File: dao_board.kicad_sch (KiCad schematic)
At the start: 37 parts, among them J1 KEY1, J10 DISH_SENSOR, J11 5V_BOOST, J12 BATTERY, J13 DISH_LED, J2 KEY2, J3 KEY3, J4 KEY4, J5 KEY5, J6 KEY6, J7 KEY7, J8 START, J9 SELECT, SW1 SW_SPDT, SW2 HX 3x4x2-2P-1.6N, U1 XIAO-nRF52840-Plus-SMD

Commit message: ネット名ミスってて直すなど
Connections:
- net KEY_LED_JV is gone; now on net KEY_LED_5V: D3.1 (K), D4.1 (K)
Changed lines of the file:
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@@
 	(wire
 		(pts
+			(xy 81.28 148.59) (xy 86.36 148.59)
+		)
+		(stroke
+			(width 0)
+			(type default)
+		)
+	)
+	(wire
+		(pts
 			(xy 204.47 31.75) (xy 204.47 40.64)
 		)
@@
 	(wire
 		(pts
-			(xy 86.36 148.59) (xy 59.69 148.59)
+			(xy 81.28 149.86) (xy 59.69 149.86)
 		)
 		(stroke
@@
 	(wire
 		(pts
+			(xy 81.28 149.86) (xy 81.28 148.59)
+		)
+		(stroke
+			(width 0)
+			(type default)
+		)
+	)
+	(wire
+		(pts
 			(xy 167.64 44.45) (xy 181.61 44.45)
 		)
@@
 	(wire
 		(pts
-			(xy 59.69 148.59) (xy 59.69 143.51)
+			(xy 59.69 149.86) (xy 59.69 143.51)
 		)
 		(stroke
@@
 		)
 	)
-	(label "KEY_LED_JV"
+	(label "KEY_LED_5V"
 		(at 107.95 148.59 180)
 		(effects
@@
 		)
 		(instances
-			(project "iidxcontroller_board"
+			(project "dao_board"
 				(path "/88e2b3bc-f15b-46e0-bc23-bfcd5e24d1de"
 					(reference "#PWR019")
@@
 		)
 		(instances
-			(project "iidxcontroller_board"
+			(project "dao_board"
 				(path "/88e2b3bc-f15b-46e0-bc23-bfcd5e24d1de"
 					(reference "J8")
@@
 		)
 		(instances
-			(project "iidxcontroller_board"
+			(project "dao_board"
 				(path "/88e2b3bc-f15b-46e0-bc23-bfcd5e24d1de"
 					(reference "C2")
@@
 		)
 		(instances
-			(project "iidxcontroller_board"
+			(project "dao_board"
 				(path "/88e2b3bc-f15b-46e0-bc23-bfcd5e24d1de"
 					(reference "D3")
@@
 		)
 		(instances
-			(project "iidxcontroller_board"
+			(project "dao_board"
 				(path "/88e2b3bc-f15b-46e0-bc23-bfcd5e24d1de"
 					(reference "H1")
@@
 		)
 		(instances
-			(project "iidxcontroller_board"
+			(project "dao_board"
 				(path "/88e2b3bc-f15b-46e0-bc23-bfcd5e24d1de"
 					(reference "D4")
@@
 		)
 		(instances
-			(project "iidxcontroller_board"
+			(project "dao_board"
 				(path "/88e2b3bc-f15b-46e0-bc23-bfcd5e24d1de"
 					(reference "SW1")
@@
 		)
 		(instances
-			(project "iidxcontroller_board"
+			(project "dao_board"
 				(path "/88e2b3bc-f15b-46e0-bc23-bfcd5e24d1de"
 					(reference "J2")
@@
 		)
 		(instances
-			(project "iidxcontroller_board"
+			(project "dao_board"
 				(path "/88e2b3bc-f15b-46e0-bc23-bfcd5e24d1de"
 					(reference "R4")
@@
 		)
 		(instances
-			(project "iidxcontroller_board"
+			(project "dao_board"
 				(path "/88e2b3bc-f15b-46e0-bc23-bfcd5e24d1de"
 					(reference "J9")
@@
 		)
 		(instances
-			(project "iidxcontroller_board"
+			(project "dao_board"
 				(path "/88e2b3bc-f15b-46e0-bc23-bfcd5e24d1de"
 					(reference "#PWR03")
@@
 		)
 		(instances
-			(project "iidxcontroller_board"
+			(project "dao_board"
 				(path "/88e2b3bc-f15b-46e0-bc23-bfcd5e24d1de"
 					(reference "U1")
@@
 		)
 		(instances
-			(project "iidxcontroller_board"
+			(project "dao_board"
 				(path "/88e2b3bc-f15b-46e0-bc23-bfcd5e24d1de"
 					(reference "H3")
@@
 		)
 		(instances
-			(project "iidxcontroller_board"
+			(project "dao_board"
 				(path "/88e2b3bc-f15b-46e0-bc23-bfcd5e24d1de"
 					(reference "#PWR08")
@@
 		)
 		(instances
-			(project "iidxcontroller_board"
+			(project "dao_board"
 				(path "/88e2b3bc-f15b-46e0-bc23-bfcd5e24d1de"
 					(reference "#PWR010")
@@
 		)
 		(instances
-			(project "iidxcontroller_board"
+			(project "dao_board"
 				(path "/88e2b3bc-f15b-46e0-bc23-bfcd5e24d1de"
 					(reference "#FLG01")
@@
 		)
 		(instances
-			(project "iidxcontroller_board"
+			(project "dao_board"
 				(path "/88e2b3bc-f15b-46e0-bc23-bfcd5e24d1de"
 					(reference "D2")
@@
 		)
 		(instances
-			(project "iidxcontroller_board"
+			(project "dao_board"
 				(path "/88e2b3bc-f15b-46e0-bc23-bfcd5e24d1de"
 					(reference "R1")
@@
 		)
 		(instances
-			(project "iidxcontroller_board"
+			(project "dao_board"
 				(path "/88e2b3bc-f15b-46e0-bc23-bfcd5e24d1de"
 					(reference "H2")
@@
 		)
 		(instances
-			(project "iidxcontroller_board"
+			(project "dao_board"
 				(path "/88e2b3bc-f15b-46e0-bc23-bfcd5e24d1de"
 					(reference "SW2")
@@
 		)
 		(instances
-			(project "iidxcontroller_board"
+			(project "dao_board"
 				(path "/88e2b3bc-f15b-46e0-bc23-bfcd5e24d1de"
 					(reference "TP5")
@@
 		)
 		(instances
-			(project "iidxcontroller_board"
+			(project "dao_board"
 				(path "/88e2b3bc-f15b-46e0-bc23-bfcd5e24d1de"
 					(reference "#FLG02")
@@
 		)
 		(instances
-			(project "iidxcontroller_board"
+			(project "dao_board"
 				(path "/88e2b3bc-f15b-46e0-bc23-bfcd5e24d1de"
 					(reference "#PWR01")
@@
 		)
 		(instances
-			(project "iidxcontroller_board"
+			(project "dao_board"
 				(path "/88e2b3bc-f15b-46e0-bc23-bfcd5e24d1de"
 					(reference "J7")
@@
 		)
 		(instances
-			(project "iidxcontroller_board"
+			(project "dao_board"
 				(path "/88e2b3bc-f15b-46e0-bc23-bfcd5e24d1de"
 					(reference "J12")
@@
 		)
 		(instances
-			(project "iidxcontroller_board"
+			(project "dao_board"
 				(path "/88e2b3bc-f15b-46e0-bc23-bfcd5e24d1de"
 					(reference "#PWR012")
@@
 		)
 		(instances
-			(project "iidxcontroller_board"
+			(project "dao_board"
 				(path "/88e2b3bc-f15b-46e0-bc23-bfcd5e24d1de"
 					(reference "TP4")
@@
 		)
 		(instances
-			(project "iidxcontroller_board"
+			(project "dao_board"
 				(path "/88e2b3bc-f15b-46e0-bc23-bfcd5e24d1de"
 					(reference "#PWR011")
@@
 		)
 		(instances
-			(project "iidxcontroller_board"
+			(project "dao_board"
 				(path "/88e2b3bc-f15b-46e0-bc23-bfcd5e24d1de"
 					(reference "J1")
@@
 		)
 		(instances
-			(project "iidxcontroller_board"
+			(project "dao_board"
 				(path "/88e2b3bc-f15b-46e0-bc23-bfcd5e24d1de"
 					(reference "TP2")
@@
 		)
 		(instances
-			(project "iidxcontroller_board"
+			(project "dao_board"
 				(path "/88e2b3bc-f15b-46e0-bc23-bfcd5e24d1de"
 					(reference "#PWR06")
@@
 		)
 		(instances
-			(project "iidxcontroller_board"
+			(project "dao_board"
 				(path "/88e2b3bc-f15b-46e0-bc23-bfcd5e24d1de"
 					(reference "#PWR05")
@@
 		)
 		(instances
-			(project "iidxcontroller_board"
+			(project "dao_board"
 				(path "/88e2b3bc-f15b-46e0-bc23-bfcd5e24d1de"
 					(reference "J3")
@@
 		)
 		(instances
-			(project "iidxcontroller_board"
+			(project "dao_board"
 				(path "/88e2b3bc-f15b-46e0-bc23-bfcd5e24d1de"
 					(reference "J5")
@@
 		)
 		(instances
-			(project "iidxcontroller_board"
+			(project "dao_board"
 				(path "/88e2b3bc-f15b-46e0-bc23-bfcd5e24d1de"
 					(reference "J6")
@@
 		)
 		(instances
-			(project "iidxcontroller_board"
+			(project "dao_board"
 				(path "/88e2b3bc-f15b-46e0-bc23-bfcd5e24d1de"
 					(reference "R3")
@@
 		)
 		(instances
-			(project "iidxcontroller_board"
+			(project "dao_board"
 				(path "/88e2b3bc-f15b-46e0-bc23-bfcd5e24d1de"
 					(reference "#PWR02")
@@
 		)
 		(instances
-			(project "iidxcontroller_board"
+			(project "dao_board"
 				(path "/88e2b3bc-f15b-46e0-bc23-bfcd5e24d1de"
 					(reference "TP6")
@@
 		)
 		(instances
-			(project "iidxcontroller_board"
+			(project "dao_board"
 				(path "/88e2b3bc-f15b-46e0-bc23-bfcd5e24d1de"
 					(reference "C1")
@@
 		)
 		(instances
-			(project "iidxcontroller_board"
+			(project "dao_board"
 				(path "/88e2b3bc-f15b-46e0-bc23-bfcd5e24d1de"
 					(reference "#PWR018")
@@
 		)
 		(instances
-			(project "iidxcontroller_board"
+			(project "dao_board"
 				(path "/88e2b3bc-f15b-46e0-bc23-bfcd5e24d1de"
 					(reference "J13")
@@
 		)
 		(instances
-			(project "iidxcontroller_board"
+			(project "dao_board"
 				(path "/88e2b3bc-f15b-46e0-bc23-bfcd5e24d1de"
 					(reference "D1")
@@
 		)
 		(instances
-			(project "iidxcontroller_board"
+			(project "dao_board"
 				(path "/88e2b3bc-f15b-46e0-bc23-bfcd5e24d1de"
 					(reference "J4")
@@
 		)
 		(instances
-			(project "iidxcontroller_board"
+			(project "dao_board"
 				(path "/88e2b3bc-f15b-46e0-bc23-bfcd5e24d1de"
 					(reference "R5")
@@
 		)
 		(instances
-			(project "iidxcontroller_board"
+			(project "dao_board"
 				(path "/88e2b3bc-f15b-46e0-bc23-bfcd5e24d1de"
 					(reference "J11")
@@
 		)
 		(instances
-			(project "iidxcontroller_board"
+			(project "dao_board"
 				(path "/88e2b3bc-f15b-46e0-bc23-bfcd5e24d1de"
 					(reference "J10")
@@
 		)
 		(instances
-			(project "iidxcontroller_board"
+			(project "dao_board"
 				(path "/88e2b3bc-f15b-46e0-bc23-bfcd5e24d1de"
 					(reference "#PWR04")
@@
 		)
 		(instances
-			(project "iidxcontroller_board"
+			(project "dao_board"
 				(path "/88e2b3bc-f15b-46e0-bc23-bfcd5e24d1de"
 					(reference "#PWR07")
@@
 		)
 		(instances
-			(project "iidxcontroller_board"
+			(project "dao_board"
 				(path "/88e2b3bc-f15b-46e0-bc23-bfcd5e24d1de"
 					(reference "#PWR016")
@@
 		)
 		(instances
-			(project "iidxcontroller_board"
+			(project "dao_board"
 				(path "/88e2b3bc-f15b-46e0-bc23-bfcd5e24d1de"
 					(reference "H4")
@@
 		)
 		(instances
-			(project "iidxcontroller_board"
+			(project "dao_board"
 				(path "/88e2b3bc-f15b-46e0-bc23-bfcd5e24d1de"
 					(reference "R2")
@@
 		)
 		(instances
-			(project "iidxcontroller_board"
+			(project "dao_board"
 				(path "/88e2b3bc-f15b-46e0-bc23-bfcd5e24d1de"
 					(reference "TP3")
@@
 		)
 		(instances
-			(project "iidxcontroller_board"
+			(project "dao_board"
 				(path "/88e2b3bc-f15b-46e0-bc23-bfcd5e24d1de"
 					(reference "#PWR017")
@@
 		)
 		(instances
-			(project "iidxcontroller_board"
+			(project "dao_board"
 				(path "/88e2b3bc-f15b-46e0-bc23-bfcd5e24d1de"
 					(reference "#PWR020")
@@
 		)
 		(instances
-			(project "iidxcontroller_board"
+			(project "dao_board"
 				(path "/88e2b3bc-f15b-46e0-bc23-bfcd5e24d1de"
 					(reference "TP1")

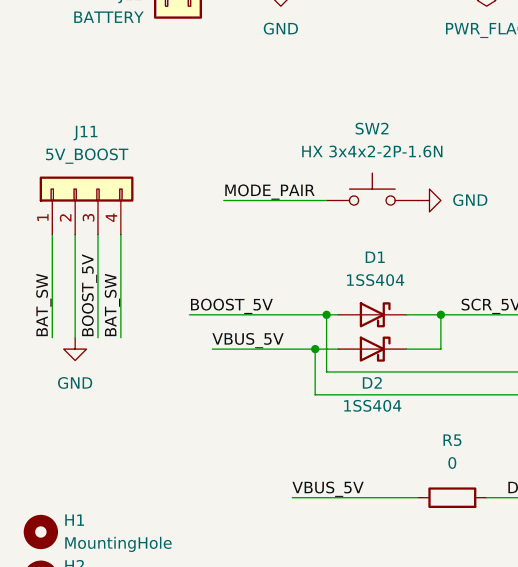
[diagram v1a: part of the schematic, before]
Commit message: 昇圧モジュールをMiniBoostに確定、フットプリントを自作する必要あり(多分ソケットにする)
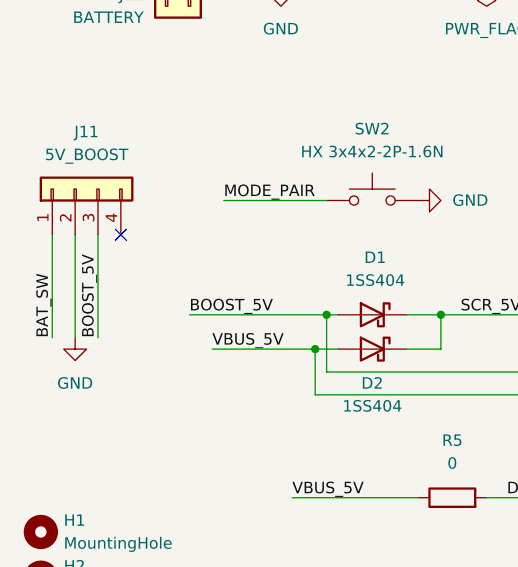
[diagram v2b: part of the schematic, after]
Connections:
- net BAT_SW: no longer J11.4 (Pin_4)
- no-connect marks 9 -> 10
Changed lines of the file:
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@@
+	)
+	(no_connect
+		(at 36.83 134.62)
 	)
 	(no_connect
@@
 	(wire
 		(pts
-			(xy 36.83 134.62) (xy 36.83 146.05)
-		)
-		(stroke
-			(width 0)
-			(type default)
-		)
-	)
-	(wire
-		(pts
 			(xy 74.93 48.26) (xy 83.82 48.26)
 		)
@@
 		(effects
 			(font
-				(size 1.27 1.27)
-			)
-			(justify left bottom)
-		)
-	)
-	(label "BAT_SW"
-		(at 36.83 146.05 90)
-		(effects
-			(font

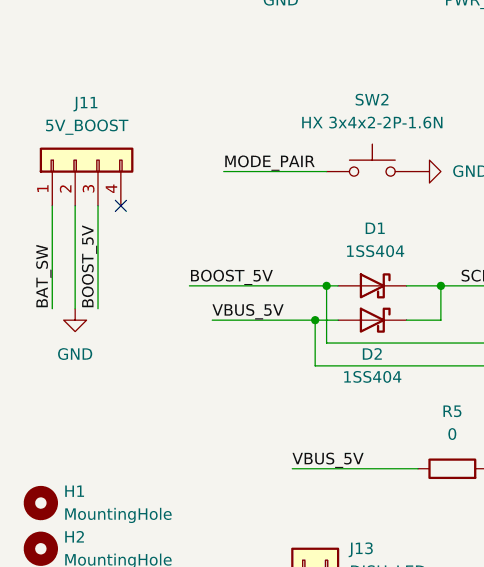
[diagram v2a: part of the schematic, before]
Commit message: フットプリント自作にあたって必要なデータをdata_tempに保存することとした、あとは回路図をモジュールに合わせて変更
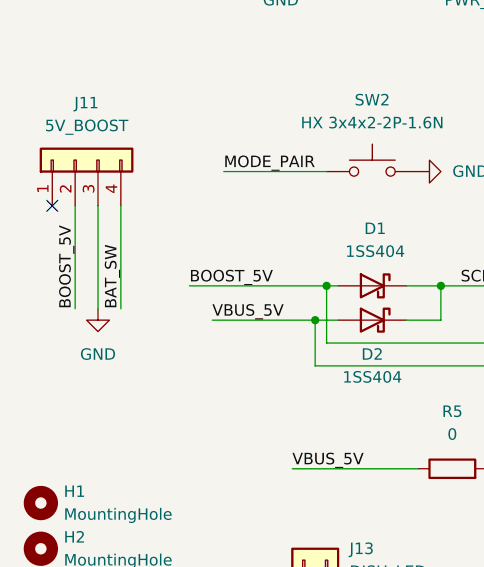
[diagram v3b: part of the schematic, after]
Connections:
- net BAT_SW: now also J11.4 (Pin_4); no longer J11.1 (Pin_1)
- net BOOST_5V: now also J11.2 (Pin_2); no longer J11.3 (Pin_3)
- net GND: now also J11.3 (Pin_3); no longer J11.2 (Pin_2)
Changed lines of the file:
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@@
 	)
 	(no_connect
-		(at 36.83 134.62)
-	)
-	(no_connect
 		(at 69.85 64.77)
 	)
@@
 	)
 	(no_connect
+		(at 29.21 134.62)
+	)
+	(no_connect
 		(at 69.85 59.69)
 	)
@@
 	(wire
 		(pts
+			(xy 31.75 134.62) (xy 31.75 146.05)
+		)
+		(stroke
+			(width 0)
+			(type default)
+		)
+	)
+	(wire
+		(pts
 			(xy 233.68 64.77) (xy 233.68 73.66)
 		)
@@
 	(wire
 		(pts
-			(xy 34.29 134.62) (xy 34.29 146.05)
-		)
-		(stroke
-			(width 0)
-			(type default)
-		)
-	)
-	(wire
-		(pts
 			(xy 190.5 31.75) (xy 190.5 40.64)
 		)
@@
 	(wire
 		(pts
-			(xy 31.75 134.62) (xy 31.75 146.05)
+			(xy 36.83 134.62) (xy 36.83 146.05)
 		)
 		(stroke
@@
 	(wire
 		(pts
+			(xy 34.29 134.62) (xy 34.29 146.05)
+		)
+		(stroke
+			(width 0)
+			(type default)
+		)
+	)
+	(wire
+		(pts
 			(xy 95.25 152.4) (xy 93.98 152.4)
 		)
@@
 	(wire
 		(pts
-			(xy 29.21 134.62) (xy 29.21 146.05)
-		)
-		(stroke
-			(width 0)
-			(type default)
-		)
-	)
-	(wire
-		(pts
 			(xy 176.53 31.75) (xy 176.53 40.64)
 		)
@@
 		)
 	)
+	(label "BOOST_5V"
+		(at 31.75 146.05 90)
+		(effects
+			(font
+				(size 1.27 1.27)
+			)
+			(justify left bottom)
+		)
+	)
 	(label "K6"
 		(at 25.4 55.88 0)
@@
 		)
 	)
-	(label "BOOST_5V"
-		(at 34.29 146.05 90)
-		(effects
-			(font
-				(size 1.27 1.27)
-			)
-			(justify left bottom)
-		)
-	)
 	(label "LED_K3"
 		(at 134.62 40.64 90)
@@
 		)
 	)
+	(label "BAT_SW"
+		(at 36.83 146.05 90)
+		(effects
+			(font
+				(size 1.27 1.27)
+			)
+			(justify left bottom)
+		)
+	)
 	(label "LED_LATCH"
 		(at 83.82 72.39 180)
@@
 		)
 	)
-	(label "BAT_SW"
-		(at 29.21 146.05 90)
-		(effects
-			(font
-				(size 1.27 1.27)
-			)
-			(justify left bottom)
-		)
-	)
 	(label "LED_K9"
 		(at 218.44 40.64 90)
@@
 	)
 	(symbol
-		(lib_id "power:GND")
-		(at 31.75 146.05 0)
-		(unit 1)
-		(body_style 1)
-		(exclude_from_sim no)
-		(in_bom yes)
-		(on_board yes)
-		(in_pos_files yes)
-		(dnp no)
-		(fields_autoplaced yes)
-		(property "Reference" "#PWR010"
-			(at 31.75 152.4 0)
-			(hide yes)
-			(show_name no)
-			(do_not_autoplace no)
-			(effects
-				(font
-					(size 1.27 1.27)
-				)
-			)
-		)
-		(property "Value" "GND"
-			(at 31.75 151.13 0)
-			(show_name no)
-			(do_not_autoplace no)
-			(effects
-				(font
-					(size 1.27 1.27)
-				)
-			)
-		)
-		(property "Footprint" ""
-			(at 31.75 146.05 0)
-			(hide yes)
-			(show_name no)
-			(do_not_autoplace no)
-			(effects
-				(font
-					(size 1.27 1.27)
-				)
-			)
-		)
-		(property "Datasheet" ""
-			(at 31.75 146.05 0)
-			(hide yes)
-			(show_name no)
-			(do_not_autoplace no)
-			(effects
-				(font
-					(size 1.27 1.27)
-				)
-			)
-		)
-		(property "Description" "Power symbol creates a global label with name \"GND\" , ground"
-			(at 31.75 146.05 0)
-			(hide yes)
-			(show_name no)
-			(do_not_autoplace no)
-			(effects
-				(font
-					(size 1.27 1.27)
-				)
-			)
-		)
-		(pin "1"
-		)
-		(instances
-			(project "dao_board"
-				(path "/88e2b3bc-f15b-46e0-bc23-bfcd5e24d1de"
-					(reference "#PWR010")
-					(unit 1)
-				)
-			)
-		)
-	)
-	(symbol
 		(lib_id "PCM_fab:PWR_FLAG")
 		(at 77.47 106.68 180)
@@
 					(unit 1)
 				)
+			)
+		)
+	)
+	(symbol
+		(lib_id "power:GND")
+		(at 34.29 146.05 0)
+		(unit 1)
+		(body_style 1)
+		(exclude_from_sim no)
+		(in_bom yes)
+		(on_board yes)
+		(in_pos_files yes)
+		(dnp no)
+		(fields_autoplaced yes)
+		(property "Reference" "#PWR010"
+			(at 34.29 152.4 0)
+			(hide yes)
+			(show_name no)
+			(do_not_autoplace no)
+			(effects
+				(font
+					(size 1.27 1.27)
+				)
+			)
+		)
+		(property "Value" "GND"
+			(at 34.29 151.13 0)
+			(show_name no)
+			(do_not_autoplace no)
+			(effects
+				(font
+					(size 1.27 1.27)
+				)
+			)
+		)
+		(property "Footprint" ""
+			(at 34.29 146.05 0)
+			(hide yes)
+			(show_name no)
+			(do_not_autoplace no)
+			(effects
+				(font
+					(size 1.27 1.27)
+				)
+			)
+		)
+		(property "Datasheet" ""
+			(at 34.29 146.05 0)
+			(hide yes)
+			(show_name no)
+			(do_not_autoplace no)
+			(effects
+				(font
+					(size 1.27 1.27)
+				)
+			)
+		)
+		(property "Description" "Power symbol creates a global label with name \"GND\" , ground"
+			(at 34.29 146.05 0)
+			(hide yes)
+			(show_name no)
+			(do_not_autoplace no)
+			(effects
+				(font
+					(size 1.27 1.27)
+				)
+			)
+		)
+		(pin "1"
+		)
+		(instances
+			(project "dao_board"
+				(path "/88e2b3bc-f15b-46e0-bc23-bfcd5e24d1de"
+					(reference "#PWR010")
+					(unit 1)
+				)

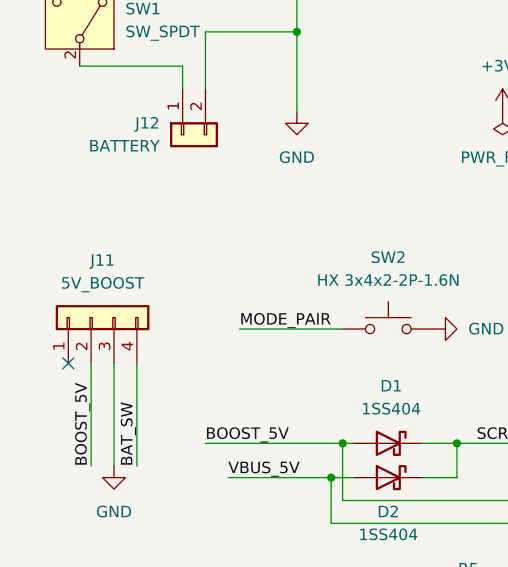
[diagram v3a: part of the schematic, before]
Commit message: 方針変更: BLE接続時でも給電はUSBから取ることにする。PS2は対応できる形にしておくのと、マイコンもGPIOが足りないので変更
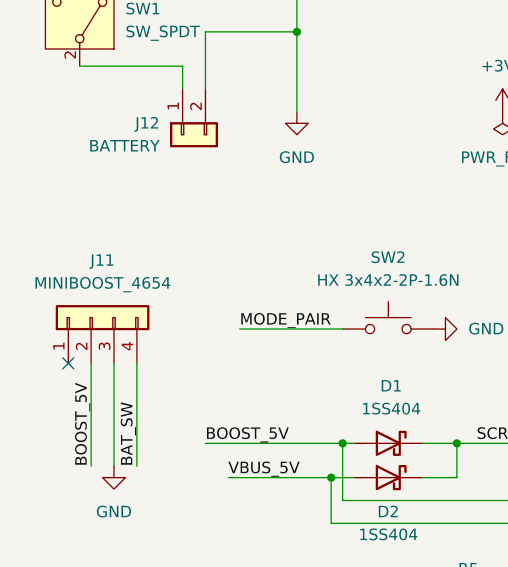
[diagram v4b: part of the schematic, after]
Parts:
- J11: value 5V_BOOST -> MINIBOOST_4654; footprint Connector_JST:JST_XH_B4B-XH-A_1x04_P2.50mm_Vertical -> Connector_PinSocket_2.54mm:PinSocket_1x04_P2.54mm_Vertical
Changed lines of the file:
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@@
 			)
 		)
-		(property "Value" "5V_BOOST"
+		(property "Value" "MINIBOOST_4654"
 			(at 33.02 125.73 90)
 			(show_name no)
@@
 			)
 		)
-		(property "Footprint" "Connector_JST:JST_XH_B4B-XH-A_1x04_P2.50mm_Vertical"
+		(property "Footprint" "Connector_PinSocket_2.54mm:PinSocket_1x04_P2.54mm_Vertical"
 			(at 31.75 129.54 0)
 			(hide yes)
